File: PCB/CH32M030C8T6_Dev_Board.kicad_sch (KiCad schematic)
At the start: 0 parts

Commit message: Added power symbols and recommended capacitors from Datasheet
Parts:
- added C1: 1μF, symbol Device:C_Polarized
- added C2, C4: 10μF, symbol Device:C_Polarized
- added C3: 100nF, symbol Device:C_Polarized
- added U1: CH32M030CxTx, Package_QFP:LQFP-48_7x7mm_P0.5mm, symbol MCU_WCH_CH32M030:CH32M030CxTx
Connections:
- new net +3.3V: C1.1, U1.34 (V_{DD33})
- new net GND: C1.2, C2.2, C3.2, C4.2, U1.36 (GND)
- new net V_{GateDrive}: C2.1, C3.1, U1.28 (V_{DD8})
- new net V_{HV}: C4.1, U1.35 (V_{HV})

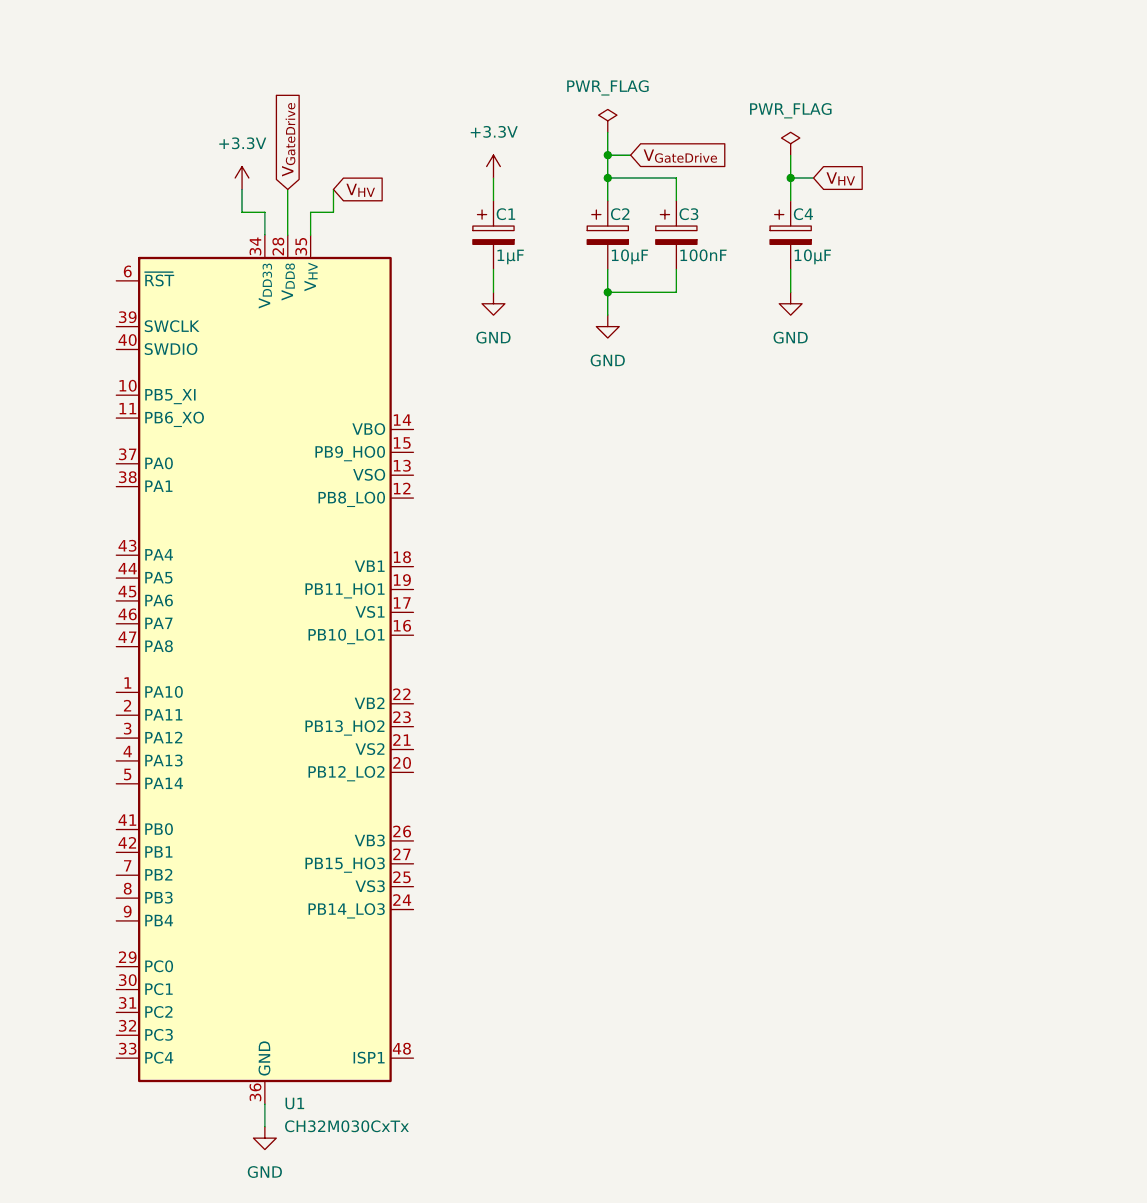
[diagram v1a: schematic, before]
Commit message: Added 2 current sense resistors and connected them to the MCU
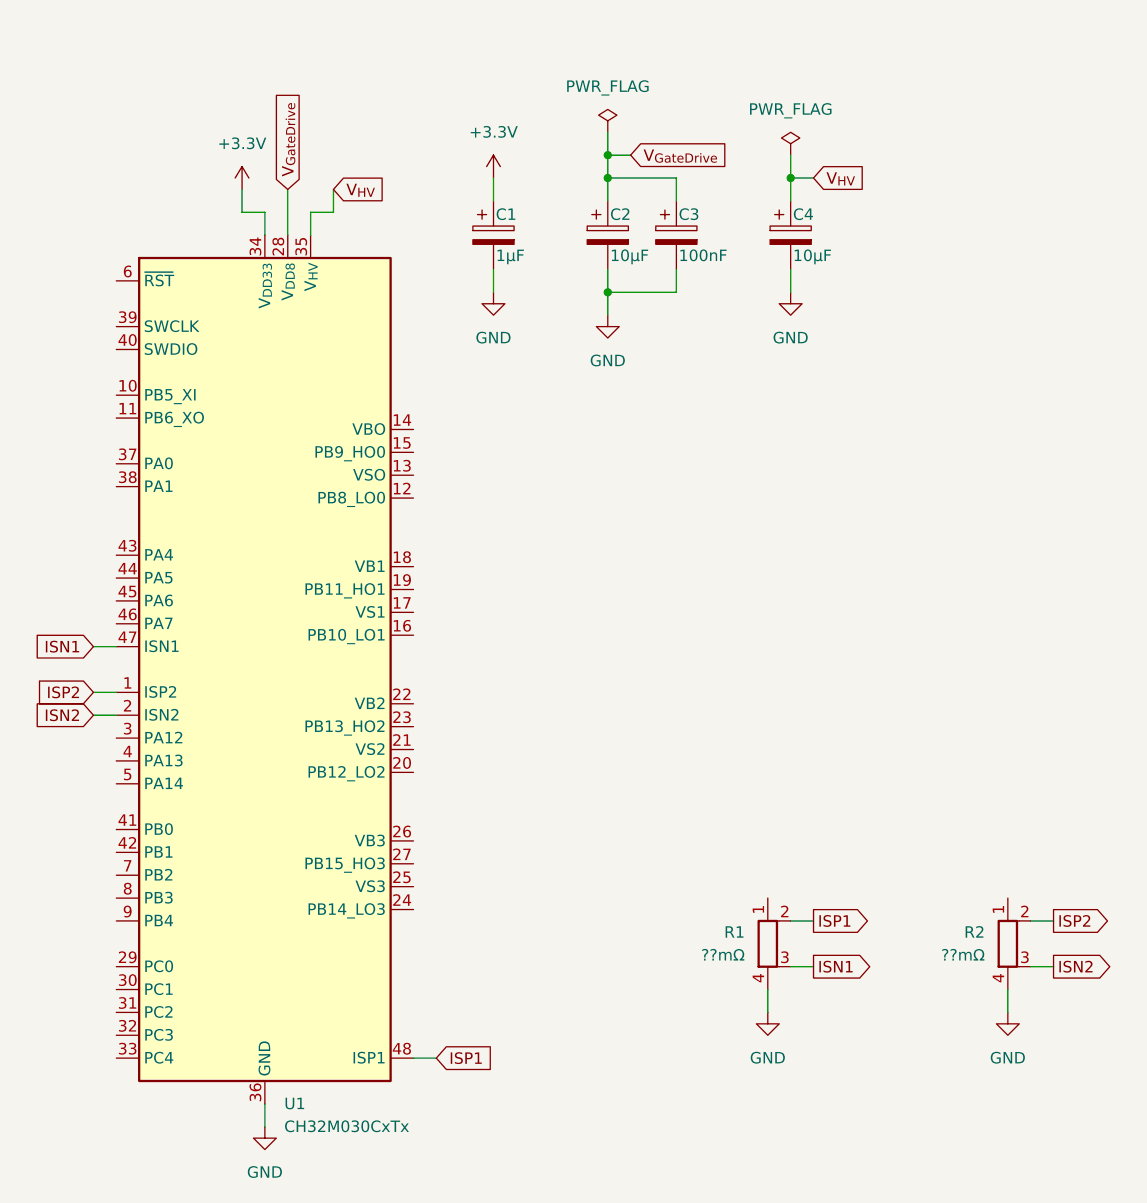
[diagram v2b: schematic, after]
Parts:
- added R1, R2: ??mΩ, symbol Device:R_Shunt
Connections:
- net GND: now also R1.4, R2.4
- net ISP2: now reaches U1.1 (PA10)
- net ISP2: now also R2.2
- net ISN2: now reaches U1.2 (PA11)
- net ISN2: now also R2.3
- net ISN1: now reaches U1.47 (PA8)
- net ISN1: now also R1.3
- net ISP1: now reaches U1.48 (ISP1)
- net ISP1: now also R1.2
